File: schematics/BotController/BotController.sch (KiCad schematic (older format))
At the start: 10 parts, among them IC1 ATMEGA644-P, SW2 reset, X1 CRYSTAL_OSSCI

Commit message: Herkulex Controller
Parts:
- added P?: UM2102 - UART2USB, symbol CONN_01X03
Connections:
- net labels added: GND, RXD0, TXD0
- wire segments 40 -> 45
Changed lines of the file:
@@
 LIBS:valves
 LIBS:BotController-cache
-LIBS:Main Controller-cache
 EELAYER 25 0
 EELAYER END
@@
 	1    0    0    -1
 $EndComp
+$Comp
+L CONN_01X03 P?
+U 1 1 571B9A9C
+P 6250 6750
+F 0 "P?" H 6250 6950 50  0000 C CNN
+F 1 "UM2102 - UART2USB" V 6350 6750 50  0000 C CNN
+F 2 "" H 6250 6750 60  0000 C CNN
+F 3 "" H 6250 6750 60  0000 C CNN
+	1    6250 6750
+	0    1    1    0
+$EndComp
+Wire Wire Line
+	6350 6550 6350 6200
+Connection ~ 6350 6200
+Wire Wire Line
+	6250 5000 6250 6550
+Wire Wire Line
+	6250 5000 6050 5000
+Wire Wire Line
+	6050 5100 6150 5100
+Wire Wire Line
+	6150 5100 6150 6550
+Text Label 6250 6550 1    39   ~ 0
+RXD0
+Text Label 6150 6550 1    39   ~ 0
+TXD0
+Text Label 6350 6550 1    39   ~ 0
+GND
 $EndSCHEMATC

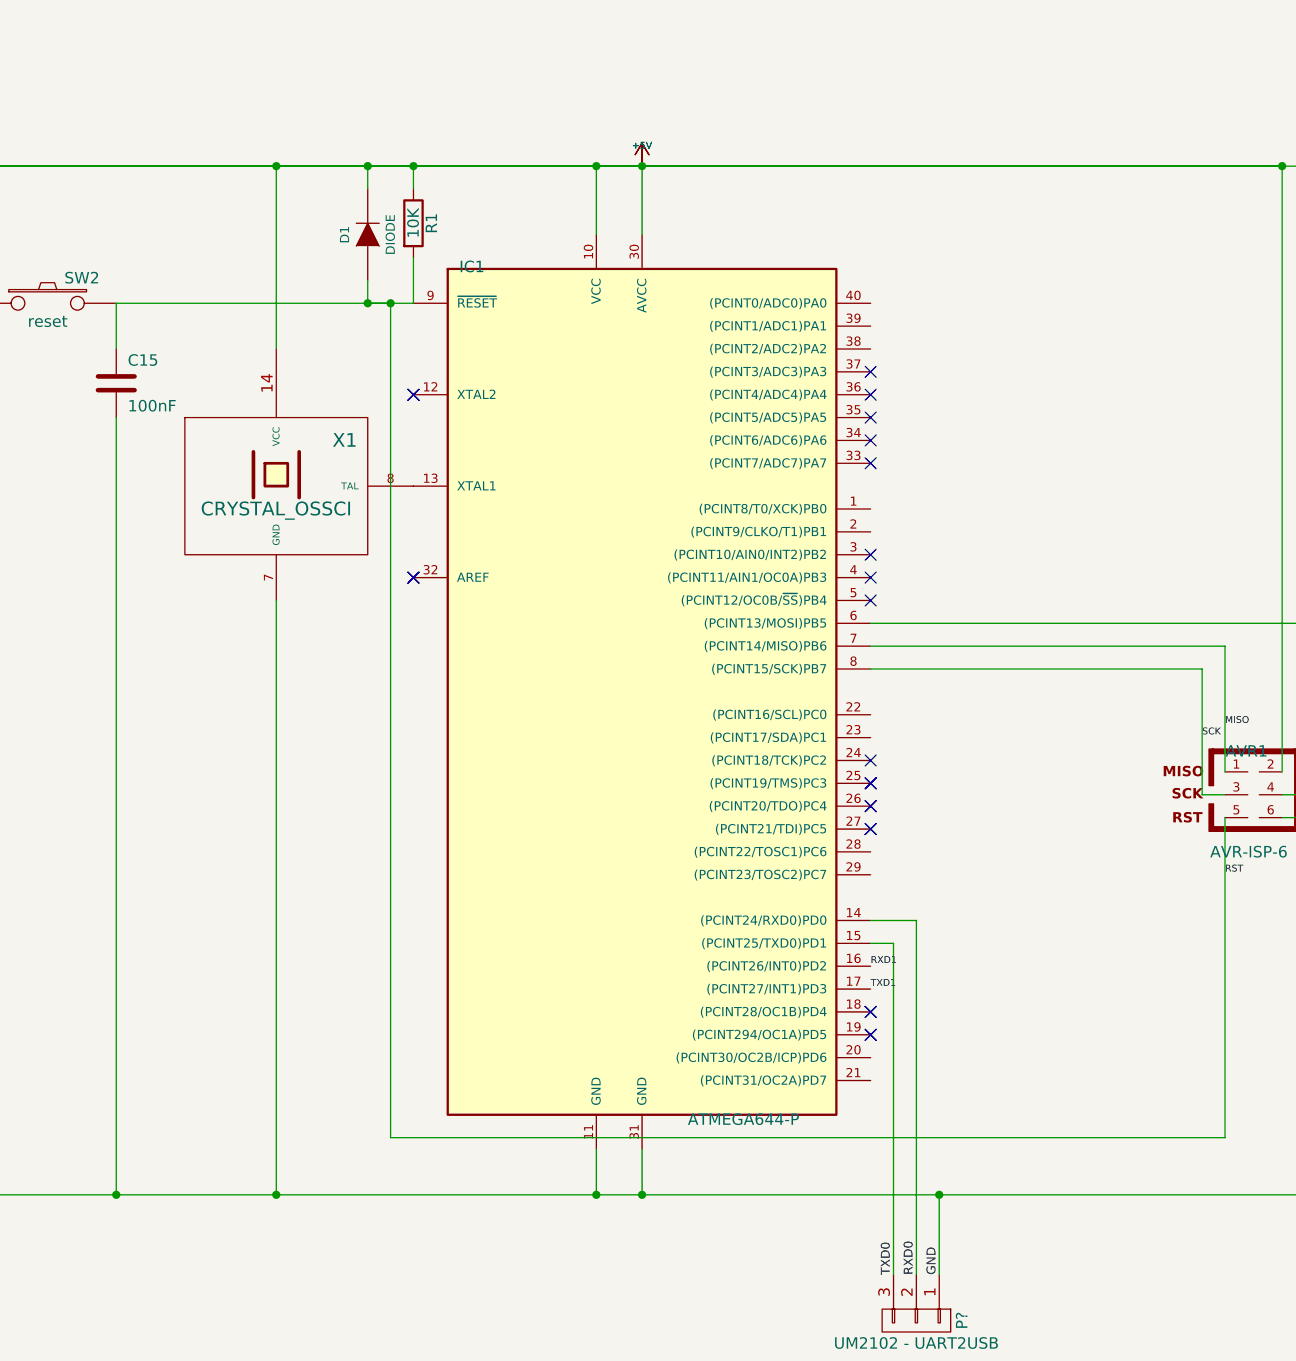
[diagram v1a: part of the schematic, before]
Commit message: Stepper Motor läuft mit Pibot treiber
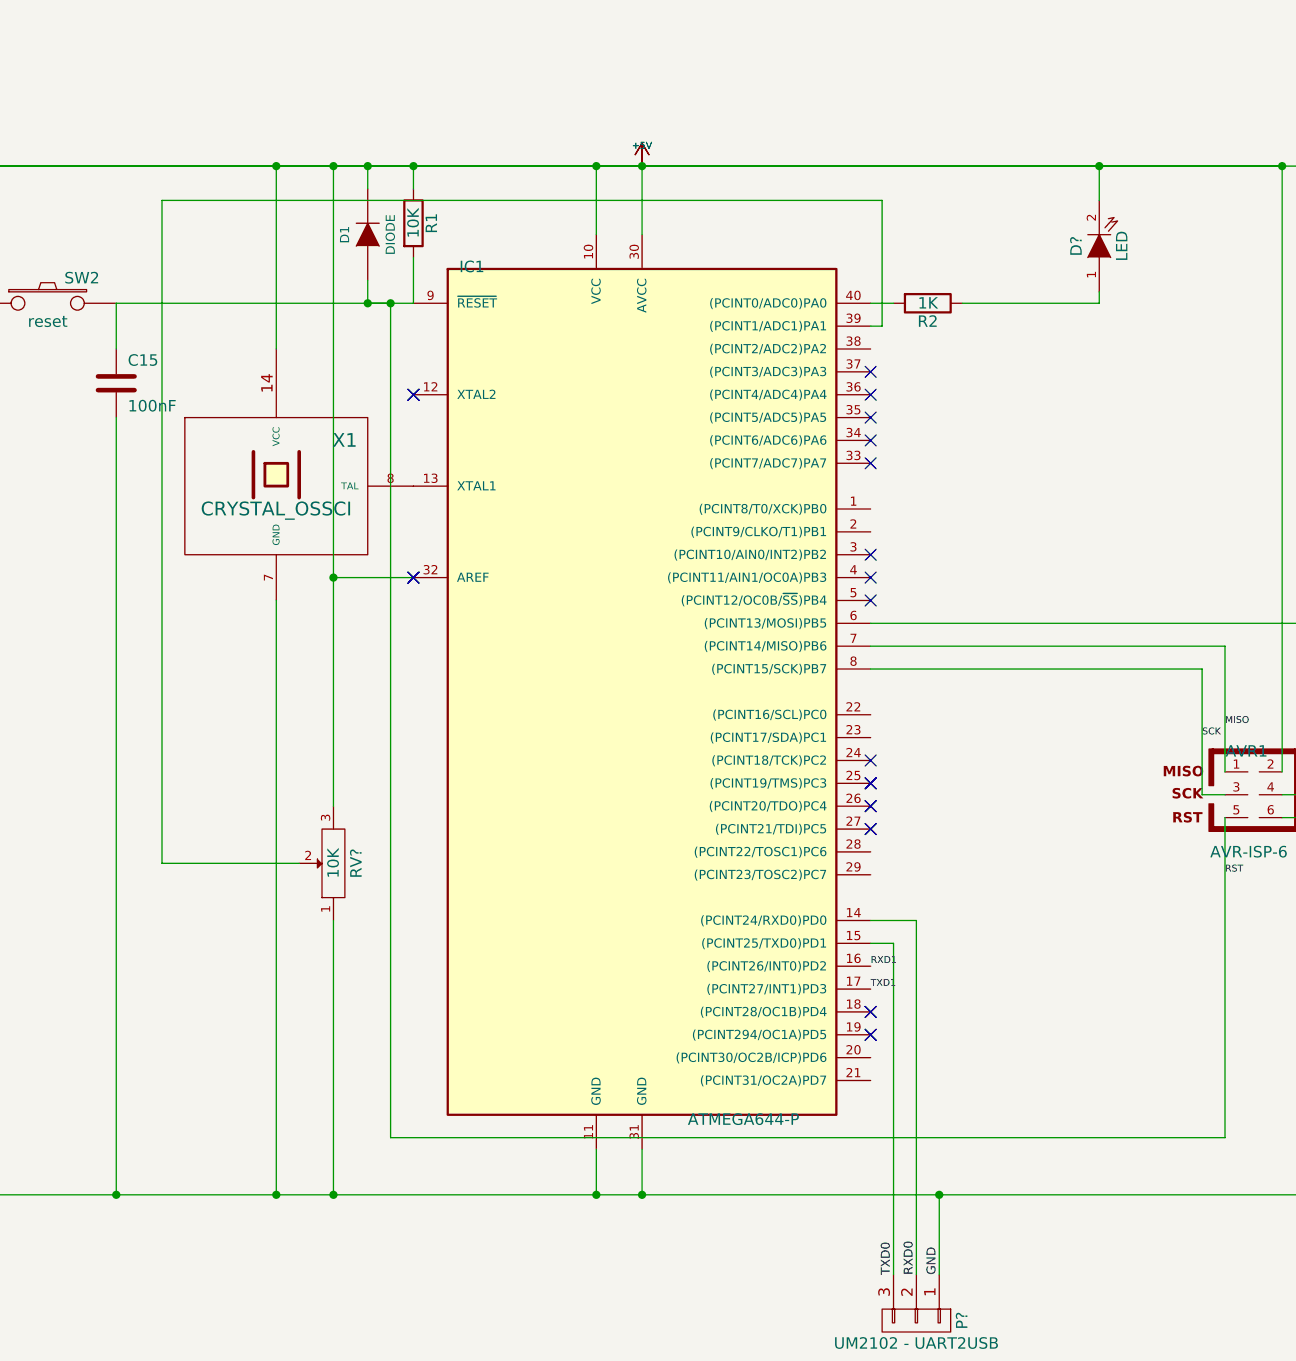
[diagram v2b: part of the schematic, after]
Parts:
- added D?: LED, symbol LED
- added R2: 1K, symbol R
- added RV?: 10K, symbol POT
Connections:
- wire segments 45 -> 57
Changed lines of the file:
@@
 Text Label 6350 6550 1    39   ~ 0
 GND
+$Comp
+L LED D?
+U 1 1 57251F35
+P 7050 2050
+F 0 "D?" H 7050 2150 50  0000 C CNN
+F 1 "LED" H 7050 1950 50  0000 C CNN
+F 2 "" H 7050 2050 60  0000 C CNN
+F 3 "" H 7050 2050 60  0000 C CNN
+	1    7050 2050
+	0    -1   -1   0
+$EndComp
+$Comp
+L R R2
+U 1 1 57251FC4
+P 6300 2300
+F 0 "R2" V 6380 2300 50  0000 C CNN
+F 1 "1K" V 6300 2300 50  0000 C CNN
+F 2 "" V 6230 2300 30  0000 C CNN
+F 3 "" H 6300 2300 30  0000 C CNN
+	1    6300 2300
+	0    1    1    0
+$EndComp
+Wire Wire Line
+	6050 2300 6150 2300
+Wire Wire Line
+	6450 2300 7050 2300
+Wire Wire Line
+	7050 2300 7050 2250
+Wire Wire Line
+	7050 1850 7050 1700
+Connection ~ 7050 1700
+Wire Wire Line
+	4050 3500 3700 3500
+Wire Wire Line
+	3700 1700 3700 4500
+Wire Wire Line
+	3700 5000 3700 6200
+Connection ~ 3700 6200
+Connection ~ 3700 1700
+Connection ~ 3700 3500
+$Comp
+L POT RV?
+U 1 1 572524E5
+P 3700 4750
+F 0 "RV?" H 3700 4650 50  0000 C CNN
+F 1 "10K" H 3700 4750 50  0000 C CNN
+F 2 "" H 3700 4750 60  0000 C CNN
+F 3 "" H 3700 4750 60  0000 C CNN
+	1    3700 4750
+	0    -1   -1   0
+$EndComp
+Wire Wire Line
+	3550 4750 2950 4750
+Wire Wire Line
+	2950 4750 2950 1850
+Wire Wire Line
+	2950 1850 6100 1850
+Wire Wire Line
+	6100 1850 6100 2400
+Wire Wire Line
+	6100 2400 6050 2400
 $EndSCHEMATC

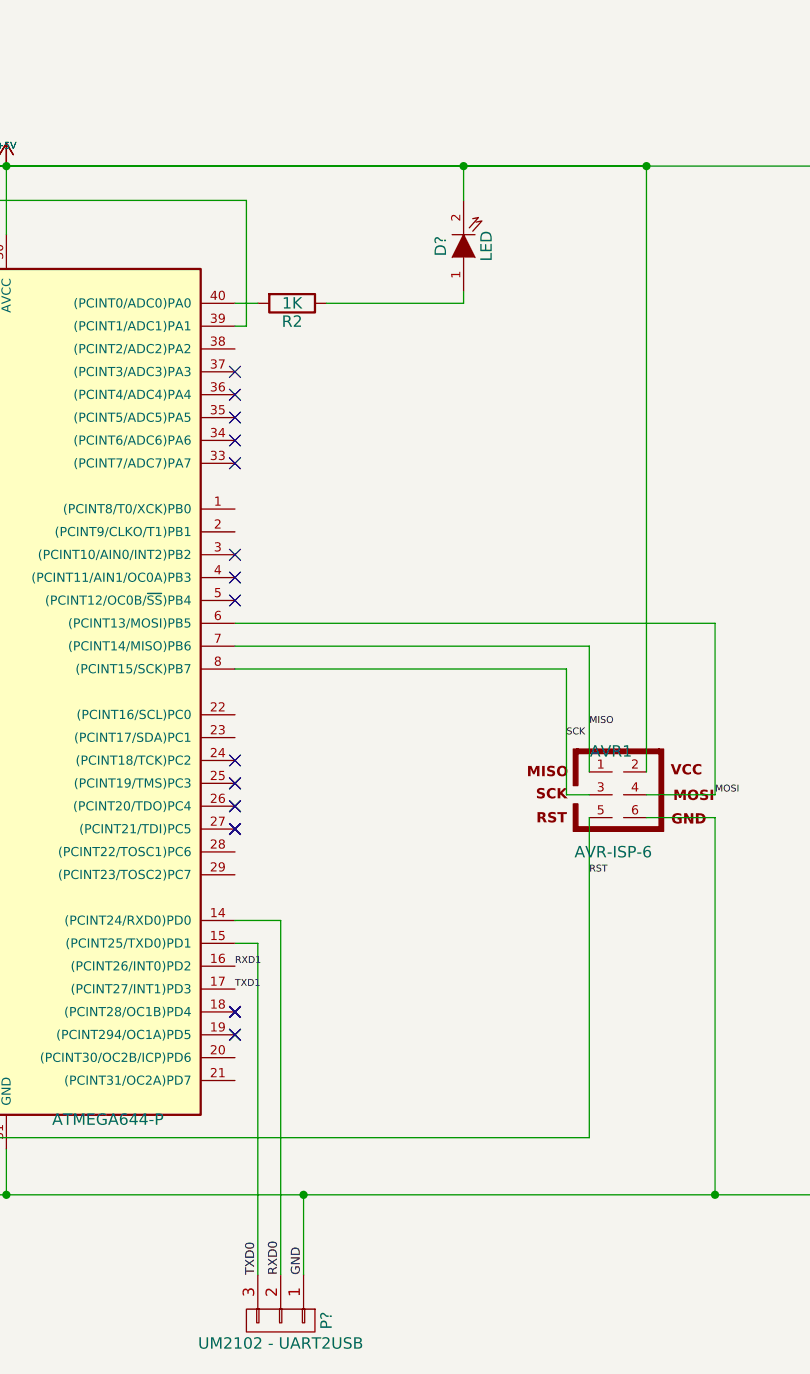
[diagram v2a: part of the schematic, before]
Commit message: AMS Sensor code als Lib
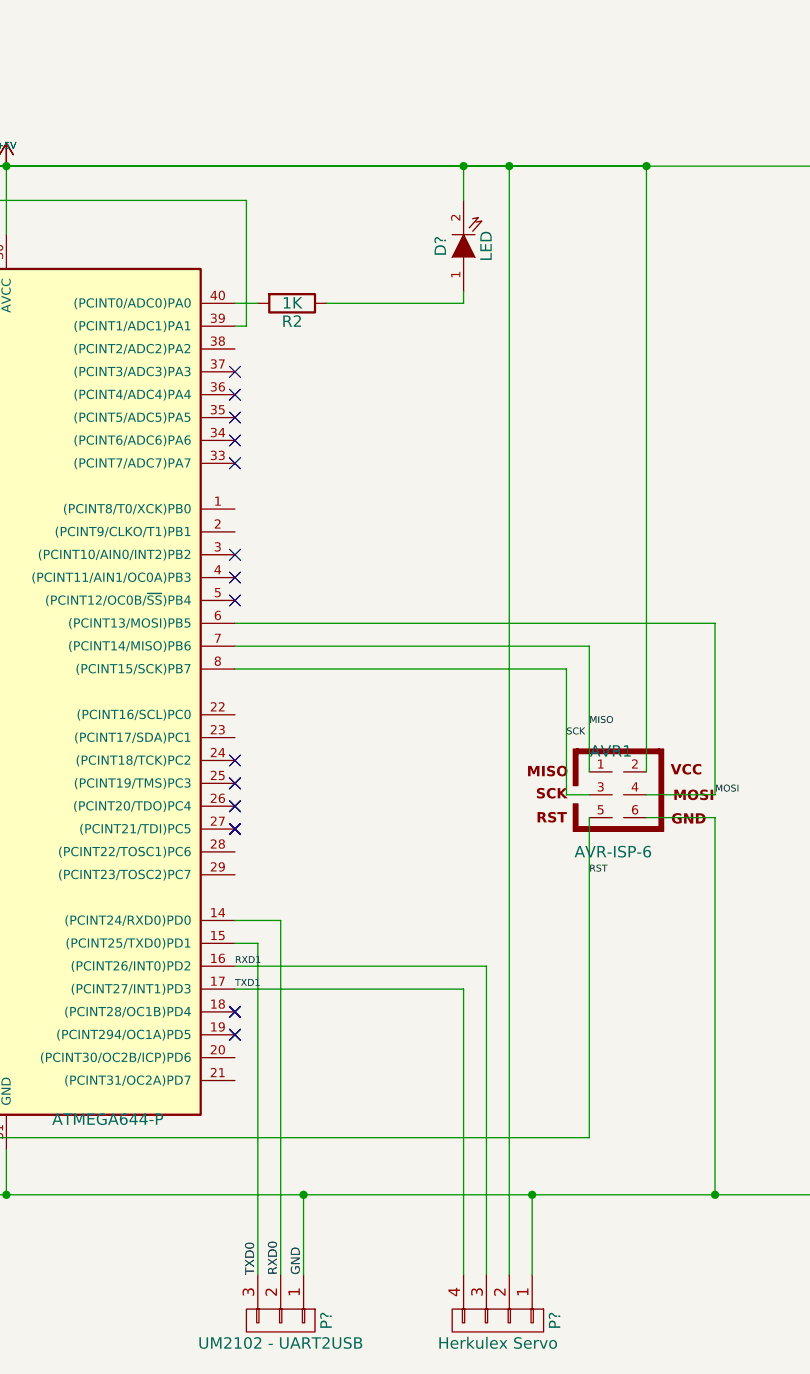
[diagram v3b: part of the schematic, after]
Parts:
- added P?: Herkulex Servo, symbol CONN_01X04
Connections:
- wire segments 57 -> 63
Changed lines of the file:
@@
 Wire Wire Line
 	6100 2400 6050 2400
+$Comp
+L CONN_01X04 P?
+U 1 1 57261EF0
+P 7200 6750
+F 0 "P?" H 7200 7000 50  0000 C CNN
+F 1 "Herkulex Servo" V 7300 6750 50  0000 C CNN
+F 2 "" H 7200 6750 60  0000 C CNN
+F 3 "" H 7200 6750 60  0000 C CNN
+	1    7200 6750
+	0    1    1    0
+$EndComp
+Wire Wire Line
+	7350 6550 7350 6200
+Connection ~ 7350 6200
+Wire Wire Line
+	7250 6550 7250 1700
+Connection ~ 7250 1700
+Wire Wire Line
+	7150 6550 7150 5200
+Wire Wire Line
+	7150 5200 6050 5200
+Wire Wire Line
+	6050 5300 7050 5300
+Wire Wire Line
+	7050 5300 7050 6550
 $EndSCHEMATC
